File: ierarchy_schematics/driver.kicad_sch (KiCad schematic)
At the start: 0 parts

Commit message: Hbridge hierarchy done.
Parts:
- added C6: 0.47u, Capacitor_SMD:C_0805_2012Metric_Pad1.18x1.45mm_HandSolder, symbol Device:C
- added D10, D20: Green LED, LED_SMD:LED_1206_3216Metric_Pad1.42x1.75mm_HandSolder, symbol Device:LED
- added D19: S1K-13-F, Diode_SMD:D_SMA, symbol Diode:1N4006
- added J14: MOSFET_out, Connector_PinHeader_2.54mm:PinHeader_1x03_P2.54mm_Vertical, symbol Connector_Generic:Conn_01x03
- added J15: Conn_01x03, Connector_PinHeader_2.54mm:PinHeader_1x03_P2.54mm_Vertical, symbol Connector_Generic:Conn_01x03
- added J16: From_MCU, Connector_PinHeader_2.54mm:PinHeader_1x06_P2.54mm_Vertical, symbol Connector_Generic:Conn_01x06
- added Q8: IRF3710, Package_TO_SOT_THT:TO-220-3_Vertical, symbol Transistor_FET:Q_Dual_NMOS_G1S2G2D2S1D1
- added R10, R9: 0, Resistor_SMD:R_0805_2012Metric_Pad1.20x1.40mm_HandSolder, symbol Device:R
- added R37: 550, Resistor_SMD:R_2512_6332Metric_Pad1.40x3.35mm_HandSolder, symbol Device:R
- added R38, R39: 10, Resistor_SMD:R_2512_6332Metric_Pad1.40x3.35mm_HandSolder, symbol Device:R
- added R40, R41, R42: 1k, Resistor_SMD:R_0805_2012Metric_Pad1.20x1.40mm_HandSolder, symbol Device:R
- added TP13, TP14, TP15: TestPoint, TestPoint:TestPoint_Loop_D2.50mm_Drill1.0mm, symbol Connector:TestPoint
- added U9: NSi6651A, Package_SO:SOIC-16W_7.5x10.3mm_P1.27mm, symbol Driver_FET:FAN7842
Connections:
- new net: R10.1, R9.2, U9.8 (VEE2)
- new net: R39.2, U9.6 (OUTL)
- new net: D19.2 (A), U9.2 (DESAT)
- new net: R38.1, U9.4 (OUTH)
- new net: D19.1 (K), R37.2
- new net: D10.1 (K), R41.2
- new net: D20.1 (K), R42.2
- new net +15_DRV2: C6.2, J15.1 (Pin_1), U9.5 (VCC2)
- new net +3V3_DRV1: J16.6 (Pin_6), R40.1, R41.1, R42.1, U9.15 (VCC1)
- new net -15_DRV2: J15.3 (Pin_3), R9.1
- new net EN: J16.5 (Pin_5), R40.2, U9.14 (~{RST}/EN)
- new net FLT: D10.2 (A), J16.4 (Pin_4), U9.13 (~{FLT})
- new net GND_DRV1: J16.1 (Pin_1), U9.11 (IN-), U9.9 (GND1)
- new net GND_DRV2: C6.1, J14.1 (Pin_1), J15.2 (Pin_2), Q8.3 (S), R10.2, TP14.1, U9.3 (GND2)
- new net IN+: J16.2 (Pin_2), U9.10 (IN+)
- new net RDY: D20.2 (A), J16.3 (Pin_3), U9.12 (RDY)
- new net drain: J14.2 (Pin_2), Q8.2 (D), R37.1, TP13.1
- new net source: J14.3 (Pin_3), Q8.1 (G), R38.2, R39.1, TP15.1, U9.7 (CLAMP)
- no-connect marks 0 -> 2

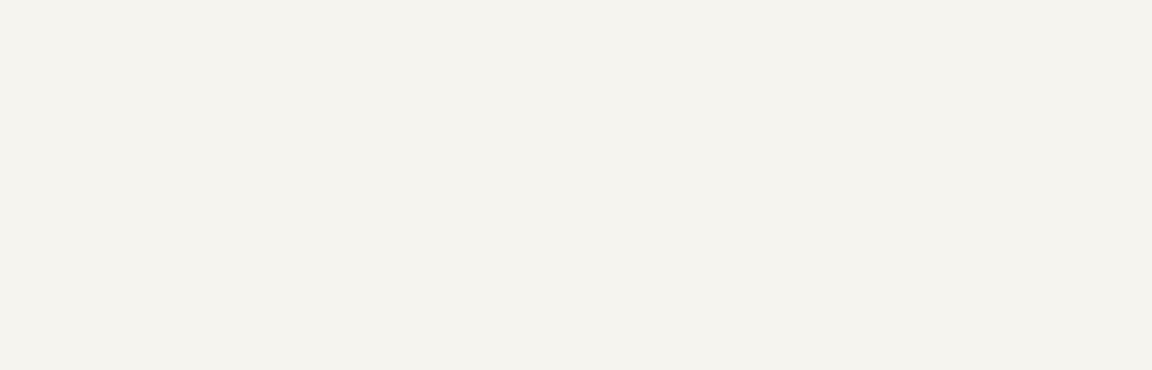
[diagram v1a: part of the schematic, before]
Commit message: Half bridge + power + MCU + optocouplers for one driver.
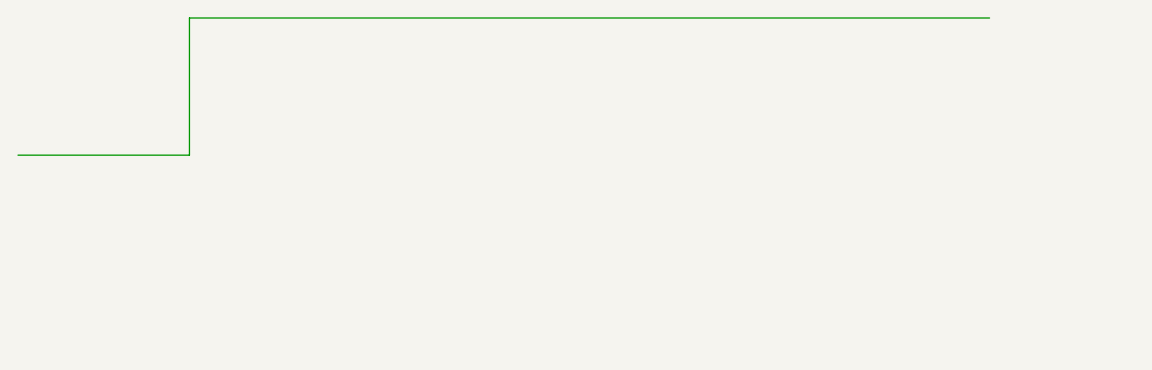
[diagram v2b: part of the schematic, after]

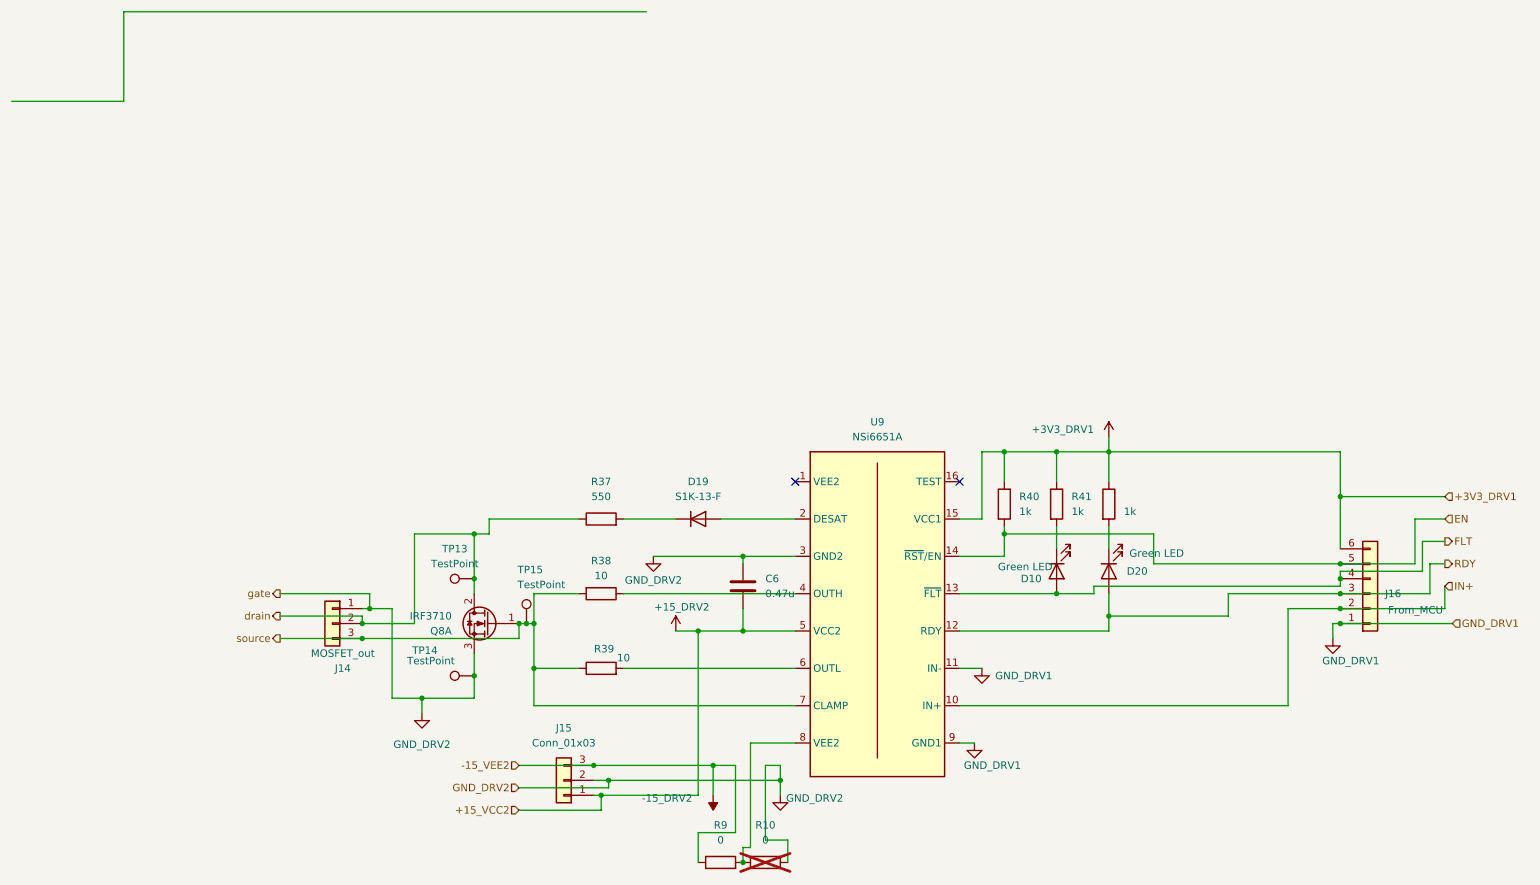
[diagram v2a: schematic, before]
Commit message: Driver PCB leds error fixed.
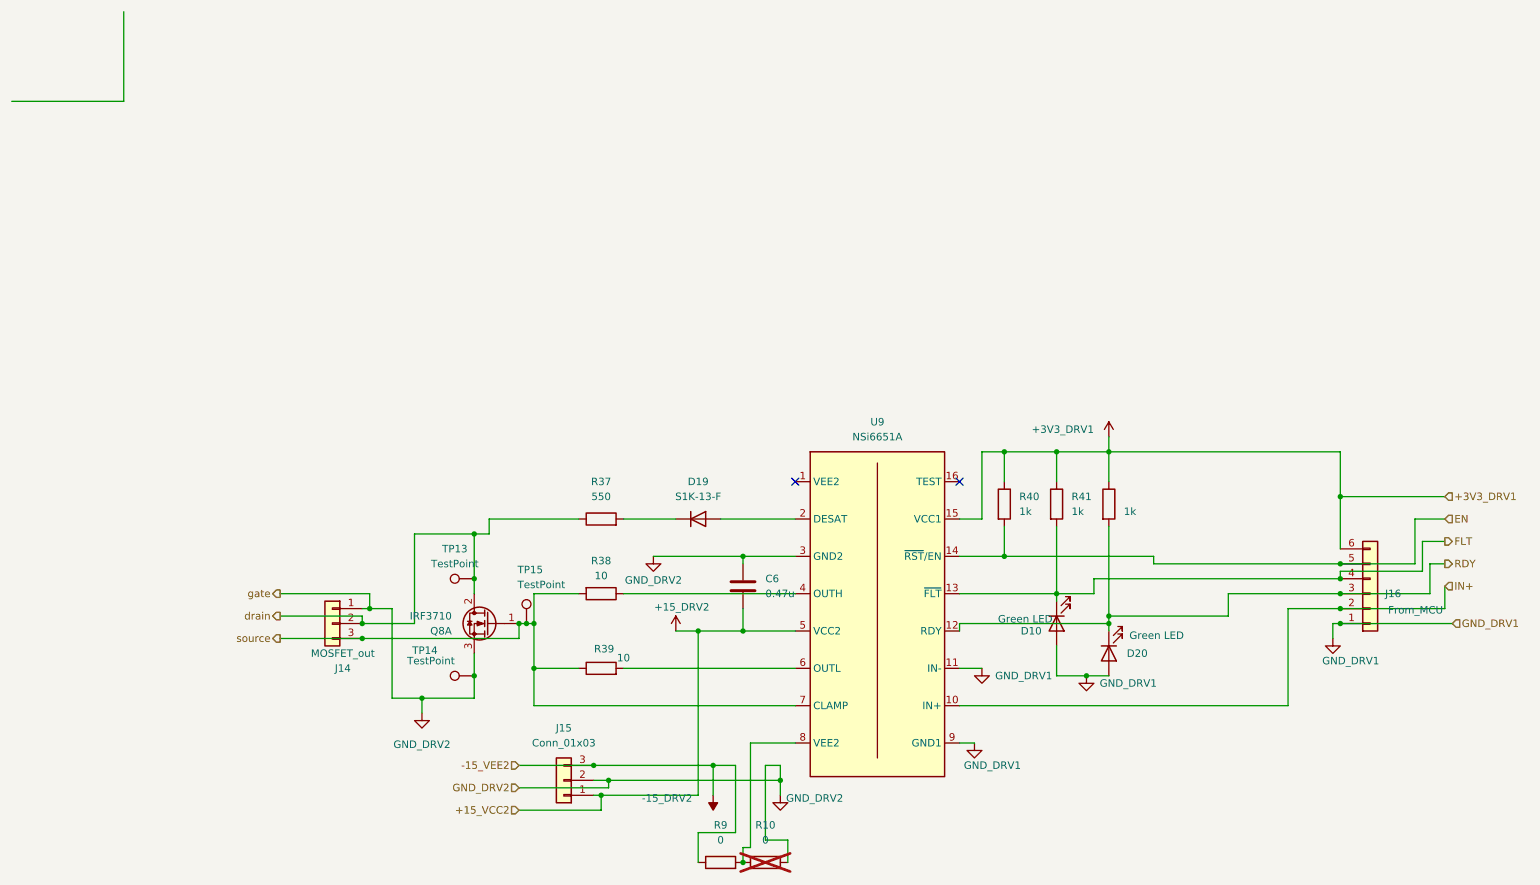
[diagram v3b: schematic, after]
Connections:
- net FLT: now also D10.1 (K), R41.2; no longer D10.2 (A)
- net GND_DRV1: now also D10.2 (A), D20.2 (A)
- net RDY: now also D20.1 (K), R42.2; no longer D20.2 (A)
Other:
- moved on the sheet: D10, D20
